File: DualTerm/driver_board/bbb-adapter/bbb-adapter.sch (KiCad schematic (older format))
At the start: 15 parts, among them P2 CONN_01X06, P3 CONN_01X06, P8 CONN_02X23, P9 CONN_02X23, U1 74LS244, U2 74LS32

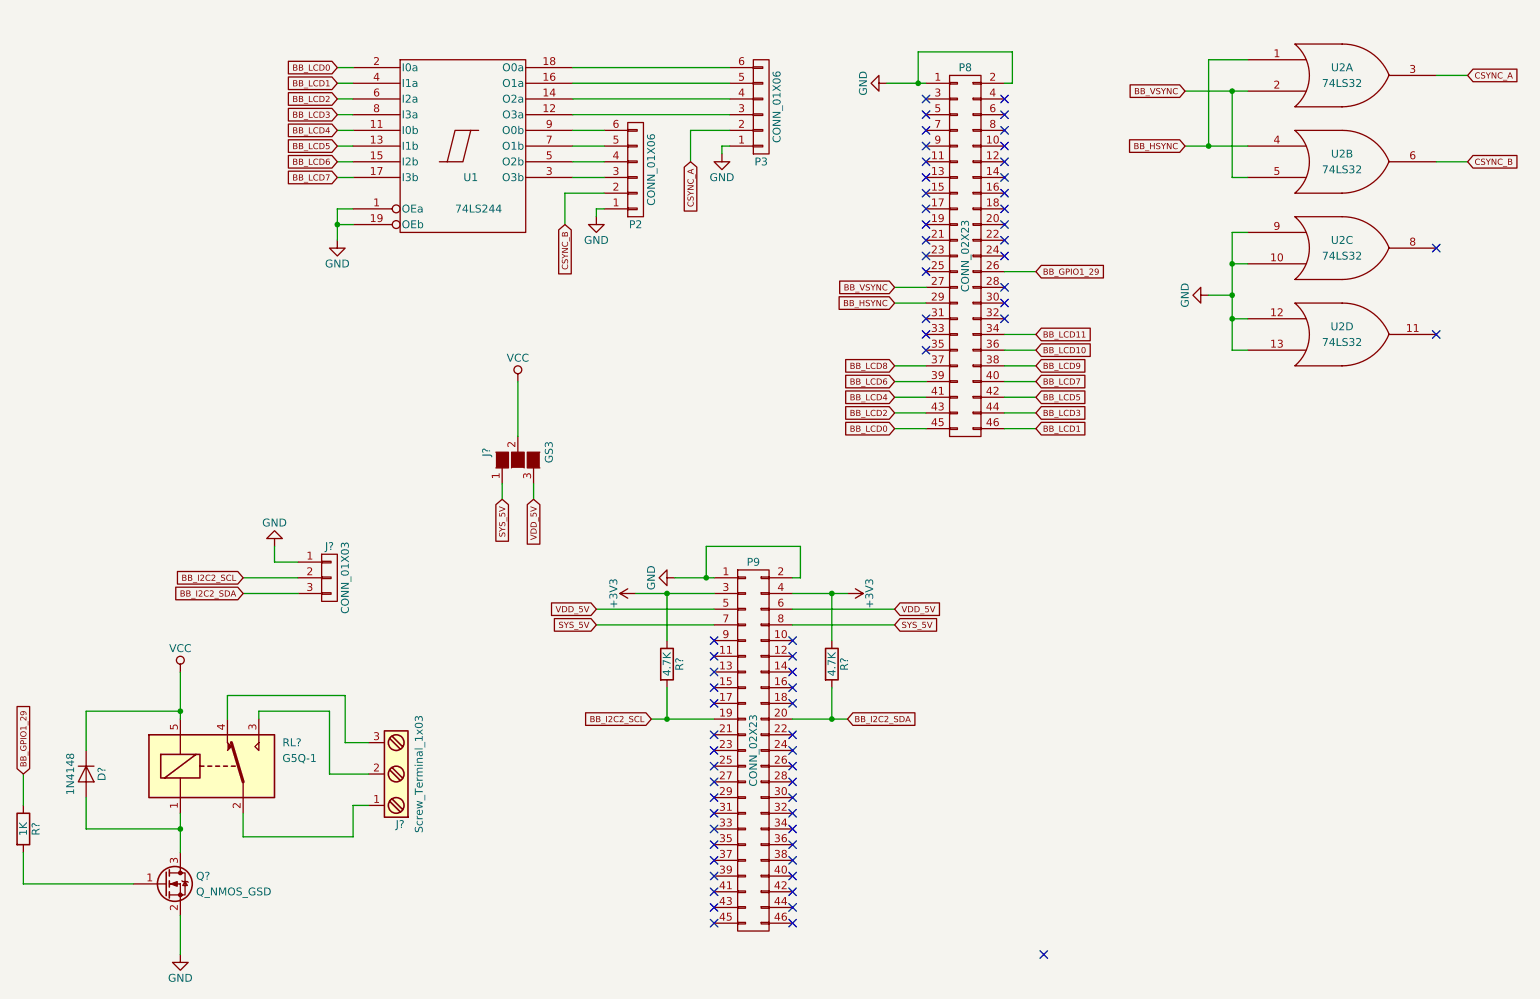
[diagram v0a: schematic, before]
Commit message: getting bbb adapter to board layout stage
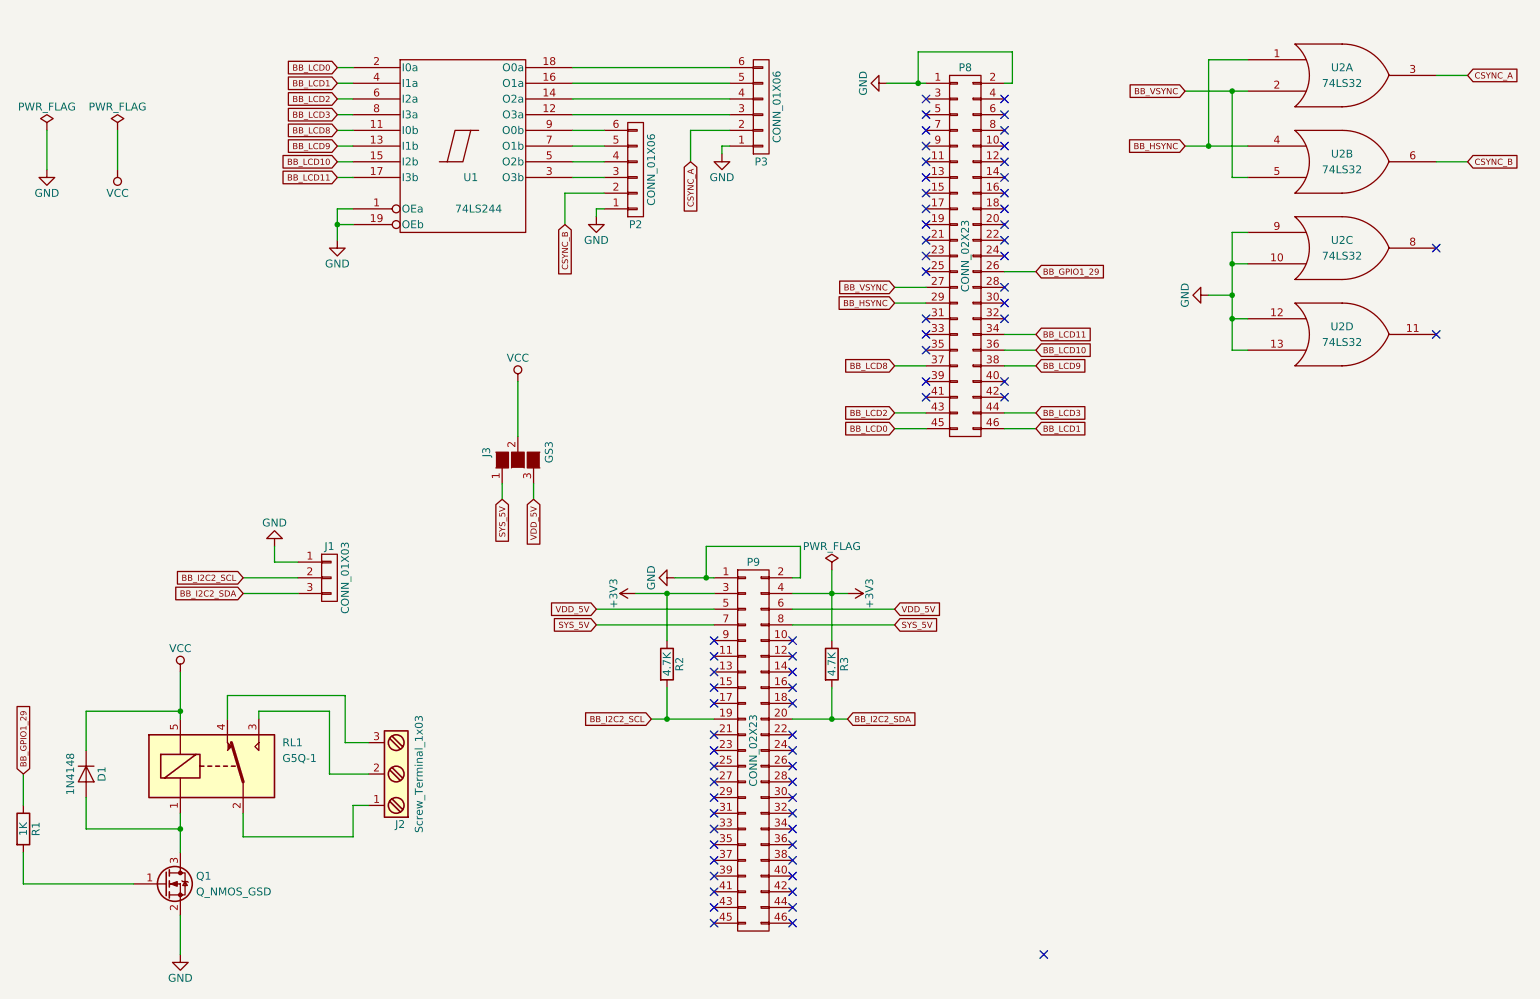
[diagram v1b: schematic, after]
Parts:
- D1: renamed from D?; footprint (none) -> Diodes_THT:D_DO-35_SOD27_P10.16mm_Horizontal
- J1: renamed from J?; footprint (none) -> Pin_Headers:Pin_Header_Angled_1x03_Pitch2.54mm
- J2: renamed from J?; footprint (none) -> Connectors_Terminal_Blocks:TerminalBlock_Pheonix_MKDS1.5-3pol
- P2, P3: footprint (none) -> Pin_Headers:Pin_Header_Angled_1x06_Pitch2.54mm
- P8, P9: footprint (none) -> Pin_Headers:Pin_Header_Straight_2x23_Pitch2.54mm
- Q1: renamed from Q?; footprint (none) -> TO_SOT_Packages_SMD:SOT-23_Handsoldering
- R1, R2, R3: renamed from R?; footprint (none) -> Resistors_THT:R_Axial_DIN0207_L6.3mm_D2.5mm_P7.62mm_Horizontal
- U1: footprint (none) -> Housings_DIP:DIP-20_W7.62mm_LongPads
- U2: footprint (none) -> Housings_DIP:DIP-14_W7.62mm_LongPads
- gave numbers to parts that had none: 2
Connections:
- net BB_LCD10: now also U1.15 (I2b)
- net BB_LCD11: now also U1.17 (I3b)
- net BB_LCD8: now also U1.11 (I0b)
- net BB_LCD9: now also U1.13 (I1b)
- net BB_LCD4: no longer names the net of P8.41 (P41)
- net BB_LCD4: no longer U1.11 (I0b)
- net BB_LCD5: no longer names the net of P8.42 (P42)
- net BB_LCD5: no longer U1.13 (I1b)
- net BB_LCD6: no longer names the net of P8.39 (P39)
- net BB_LCD6: no longer U1.15 (I2b)
- net BB_LCD7: no longer names the net of P8.40 (P40)
- net BB_LCD7: no longer U1.17 (I3b)
- no-connect marks 68 -> 72

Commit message: initial PCB layout
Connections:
- net BB_LCD0: now also U1.8 (I3a); no longer U1.2 (I0a)
- net BB_LCD1: now also U1.6 (I2a); no longer U1.4 (I1a)
- net BB_LCD10: now also U1.13 (I1b); no longer U1.15 (I2b)
- net BB_LCD11: now also U1.11 (I0b); no longer U1.17 (I3b)
- net BB_LCD2: now also U1.4 (I1a); no longer U1.6 (I2a)
- net BB_LCD3: now also U1.2 (I0a); no longer U1.8 (I3a)
- net BB_LCD8: now also U1.17 (I3b); no longer U1.11 (I0b)
- net BB_LCD9: now also U1.15 (I2b); no longer U1.13 (I1b)
- net at U1.12 (O3a): now also P3.6 (P6); no longer P3.3 (P3)
- net at U1.14 (O2a): now also P3.5 (P5); no longer P3.4 (P4)
- net at U1.16 (O1a): now also P3.4 (P4); no longer P3.5 (P5)
- net at U1.18 (O0a): now also P3.3 (P3); no longer P3.6 (P6)
- net at U1.3 (O3b): now also P2.6 (P6); no longer P2.3 (P3)
- net at U1.5 (O2b): now also P2.5 (P5); no longer P2.4 (P4)
- net at U1.7 (O1b): now also P2.4 (P4); no longer P2.5 (P5)
- net at U1.9 (O0b): now also P2.3 (P3); no longer P2.6 (P6)
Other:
- moved on the sheet: P2, P3
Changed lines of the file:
@@
 	1    0    0    -1
 $EndComp
+Text GLabel 2850 2100 0    39   Input ~ 0
+BB_LCD0
+Text GLabel 2850 2000 0    39   Input ~ 0
+BB_LCD1
+Text GLabel 2850 1900 0    39   Input ~ 0
+BB_LCD2
 Text GLabel 2850 1800 0    39   Input ~ 0
-BB_LCD0
-Text GLabel 2850 1900 0    39   Input ~ 0
-BB_LCD1
-Text GLabel 2850 2000 0    39   Input ~ 0
-BB_LCD2
-Text GLabel 2850 2100 0    39   Input ~ 0
 BB_LCD3
+Text GLabel 2850 2500 0    39   Input ~ 0
+BB_LCD8
+Text GLabel 2850 2400 0    39   Input ~ 0
+BB_LCD9
+Text GLabel 2850 2300 0    39   Input ~ 0
+BB_LCD10
 Text GLabel 2850 2200 0    39   Input ~ 0
-BB_LCD8
-Text GLabel 2850 2300 0    39   Input ~ 0
-BB_LCD9
-Text GLabel 2850 2400 0    39   Input ~ 0
-BB_LCD10
-Text GLabel 2850 2500 0    39   Input ~ 0
 BB_LCD11
 $Comp
@@
 L CONN_01X06 P3
 U 1 1 5956C702
-P 5550 2050
-F 0 "P3" H 5550 2400 50  0000 C CNN
-F 1 "CONN_01X06" V 5650 2050 50  0000 C CNN
-F 2 "Pin_Headers:Pin_Header_Angled_1x06_Pitch2.54mm" H 5550 2050 50  0001 C CNN
-F 3 "" H 5550 2050 50  0000 C CNN
-	1    5550 2050
-	1    0    0    1
+P 5550 1850
+F 0 "P3" H 5550 2200 50  0000 C CNN
+F 1 "CONN_01X06" V 5650 1850 50  0000 C CNN
+F 2 "Pin_Headers:Pin_Header_Angled_1x06_Pitch2.54mm" H 5550 1850 50  0001 C CNN
+F 3 "" H 5550 1850 50  0000 C CNN
+	1    5550 1850
+	1    0    0    -1
 $EndComp
 $Comp
 L CONN_01X06 P2
 U 1 1 5956C76B
-P 4750 2450
-F 0 "P2" H 4750 2800 50  0000 C CNN
-F 1 "CONN_01X06" V 4850 2450 50  0000 C CNN
-F 2 "Pin_Headers:Pin_Header_Angled_1x06_Pitch2.54mm" H 4750 2450 50  0001 C CNN
-F 3 "" H 4750 2450 50  0000 C CNN
-	1    4750 2450
-	1    0    0    1
+P 5550 2600
+F 0 "P2" H 5550 2950 50  0000 C CNN
+F 1 "CONN_01X06" V 5650 2600 50  0000 C CNN
+F 2 "Pin_Headers:Pin_Header_Angled_1x06_Pitch2.54mm" H 5550 2600 50  0001 C CNN
+F 3 "" H 5550 2600 50  0000 C CNN
+	1    5550 2600
+	1    0    0    -1
 $EndComp
 $Comp
 L GND #PWR03
 U 1 1 5956CB69
-P 5300 2350
-F 0 "#PWR03" H 5300 2100 50  0001 C CNN
-F 1 "GND" H 5300 2200 50  0000 C CNN
-F 2 "" H 5300 2350 50  0000 C CNN
-F 3 "" H 5300 2350 50  0000 C CNN
-	1    5300 2350
-	1    0    0    -1
+P 5000 1600
+F 0 "#PWR03" H 5000 1350 50  0001 C CNN
+F 1 "GND" H 5000 1450 50  0000 C CNN
+F 2 "" H 5000 1600 50  0000 C CNN
+F 3 "" H 5000 1600 50  0000 C CNN
+	1    5000 1600
+	0    1    1    0
 $EndComp
 $Comp
 L GND #PWR04
 U 1 1 5956CB89
-P 4500 2750
-F 0 "#PWR04" H 4500 2500 50  0001 C CNN
-F 1 "GND" H 4500 2600 50  0000 C CNN
-F 2 "" H 4500 2750 50  0000 C CNN
-F 3 "" H 4500 2750 50  0000 C CNN
-	1    4500 2750
-	1    0    0    -1
+P 5250 2300
+F 0 "#PWR04" H 5250 2050 50  0001 C CNN
+F 1 "GND" H 5250 2150 50  0000 C CNN
+F 2 "" H 5250 2300 50  0000 C CNN
+F 3 "" H 5250 2300 50  0000 C CNN
+	1    5250 2300
+	-1   0    0    1
 $EndComp
 Text GLabel 10050 1850 2    39   Input ~ 0
@@
 Text GLabel 10050 2400 2    39   Input ~ 0
 CSYNC_B
-Text GLabel 5100 2400 3    39   Input ~ 0
+Text GLabel 5250 1700 0    39   Input ~ 0
 CSYNC_A
-Text GLabel 4300 2800 3    39   Input ~ 0
+Text GLabel 5250 2450 0    39   Input ~ 0
 CSYNC_B
 $Comp
@@
 	2950 2200 2850 2200
 Wire Wire Line
-	4350 2500 4550 2500
-Wire Wire Line
-	4550 2400 4350 2400
-Wire Wire Line
-	4350 2300 4550 2300
-Wire Wire Line
-	4550 2200 4350 2200
-Wire Wire Line
 	5350 2100 4350 2100
 Wire Wire Line
@@
 Wire Wire Line
 	9850 1850 10050 1850
-Wire Wire Line
-	4500 2750 4500 2700
-Wire Wire Line
-	4500 2700 4550 2700
-Wire Wire Line
-	5300 2350 5300 2300
-Wire Wire Line
-	5300 2300 5350 2300
-Wire Wire Line
-	4300 2800 4300 2600
-Wire Wire Line
-	4300 2600 4550 2600
-Wire Wire Line
-	5100 2400 5100 2200
-Wire Wire Line
-	5100 2200 5350 2200
 Wire Wire Line
 	8550 3250 8400 3250
@@
 	7100 3500 7300 3500
 Wire Wire Line
-	5250 5150 4750 5150
+	4750 5150 5250 5150
 Wire Wire Line
 	4850 5950 5250 5950
@@
 NoConn ~ 6600 3900
 NoConn ~ 6600 3800
+Wire Wire Line
+	5250 1700 5350 1700
+Wire Wire Line
+	5350 1600 5000 1600
+Wire Wire Line
+	5250 2300 5250 2350
+Wire Wire Line
+	5250 2350 5350 2350
+Wire Wire Line
+	5350 2450 5250 2450
+Wire Wire Line
+	4350 2500 4500 2500
+Wire Wire Line
+	4500 2500 4500 2850
+Wire Wire Line
+	4500 2850 5350 2850
+Wire Wire Line
+	4350 2400 4550 2400
+Wire Wire Line
+	4550 2400 4550 2750
+Wire Wire Line
+	4550 2750 5350 2750
+Wire Wire Line
+	4350 2300 4600 2300
+Wire Wire Line
+	4600 2300 4600 2650
+Wire Wire Line
+	4600 2650 5350 2650
+Wire Wire Line
+	4350 2200 4650 2200
+Wire Wire Line
+	4650 2200 4650 2550
+Wire Wire Line
+	4650 2550 5350 2550
 $EndSCHEMATC

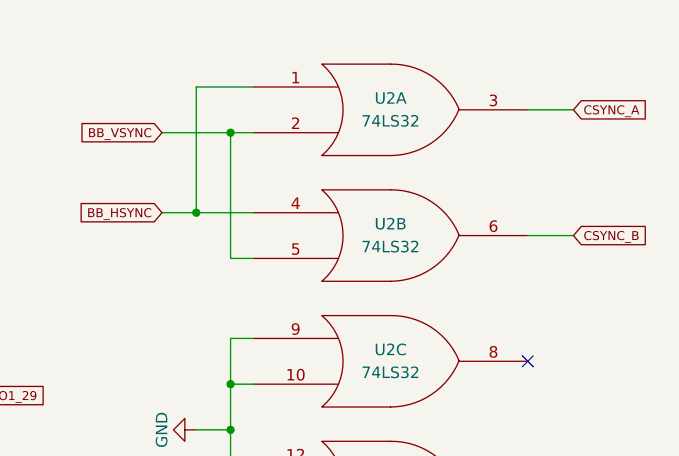
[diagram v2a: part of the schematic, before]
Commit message: board ordered
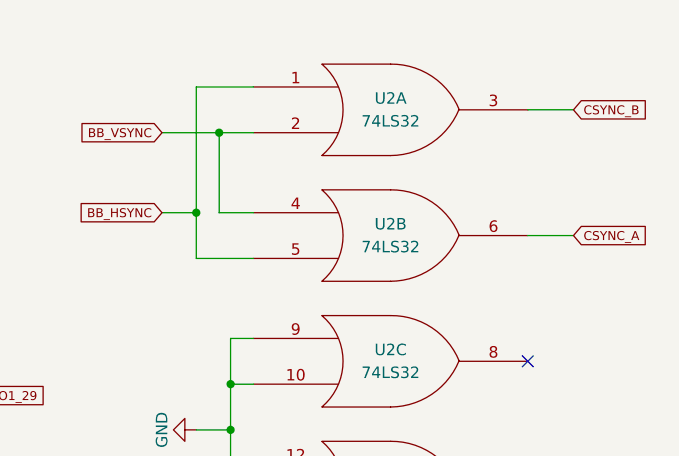
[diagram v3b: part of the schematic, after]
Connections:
- net BB_HSYNC: now also U2.5; no longer U2.4
- net BB_VSYNC: now also U2.4; no longer U2.5
- net CSYNC_A: now also U2.6; no longer U2.3
- net CSYNC_B: now also U2.3; no longer U2.6
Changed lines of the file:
@@
-	1    0    0    -1
-$EndComp
-$Comp
-L 74LS32 U2
-U 2 1 5956C157
-P 9250 2400
-F 0 "U2" H 9250 2450 50  0000 C CNN
-F 1 "74LS32" H 9250 2350 50  0000 C CNN
-F 2 "Housings_DIP:DIP-14_W7.62mm_LongPads" H 9250 2400 50  0001 C CNN
-F 3 "" H 9250 2400 50  0000 C CNN
-	2    9250 2400
 	1    0    0    -1
 $EndComp
@@
 	-1   0    0    1
 $EndComp
+Text GLabel 10050 2400 2    39   Input ~ 0
+CSYNC_A
 Text GLabel 10050 1850 2    39   Input ~ 0
-CSYNC_A
-Text GLabel 10050 2400 2    39   Input ~ 0
 CSYNC_B
 Text GLabel 5250 1700 0    39   Input ~ 0
@@
 	6400 4000 6600 4000
 Wire Wire Line
-	8250 2300 8650 2300
-Wire Wire Line
 	8250 1950 8650 1950
 Wire Wire Line
 	8650 1750 8400 1750
 Wire Wire Line
-	8400 1750 8400 2300
+	8400 1750 8400 2500
 Connection ~ 8400 2300
-Wire Wire Line
-	8650 2500 8550 2500
-Wire Wire Line
-	8550 2500 8550 1950
-Connection ~ 8550 1950
 Wire Wire Line
 	2850 2700 2850 2900
@@
 Wire Wire Line
 	4650 2550 5350 2550
+$Comp
+L 74LS32 U2
+U 2 1 5956C157
+P 9250 2400
+F 0 "U2" H 9250 2450 50  0000 C CNN
+F 1 "74LS32" H 9250 2350 50  0000 C CNN
+F 2 "Housings_DIP:DIP-14_W7.62mm_LongPads" H 9250 2400 50  0001 C CNN
+F 3 "" H 9250 2400 50  0000 C CNN
+	2    9250 2400
+	1    0    0    -1
+$EndComp
+Wire Wire Line
+	8400 2300 8250 2300
+Wire Wire Line
+	8400 2500 8650 2500
+Wire Wire Line
+	8650 2300 8500 2300
+Wire Wire Line
+	8500 2300 8500 1950
+Connection ~ 8500 1950
 $EndSCHEMATC
